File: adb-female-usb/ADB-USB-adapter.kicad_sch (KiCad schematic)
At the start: 2 parts

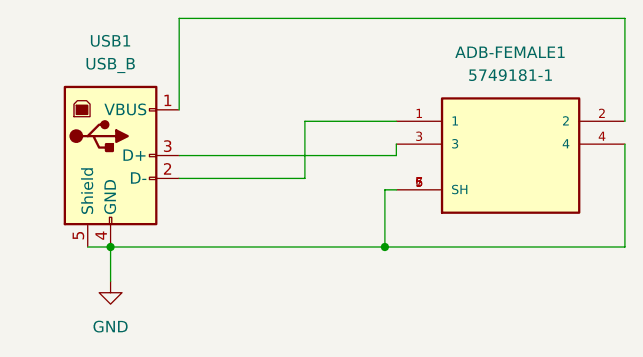
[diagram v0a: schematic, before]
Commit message: switched D+/D- on USB PCB, isolated shield from ground
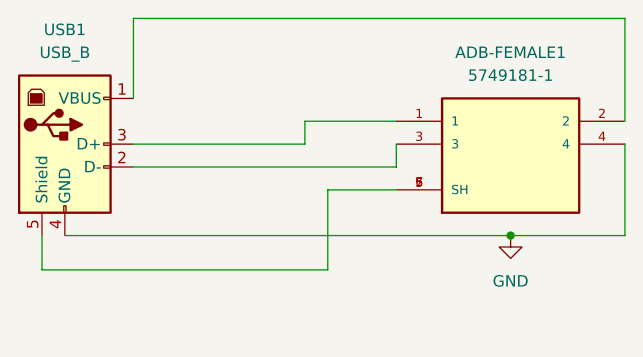
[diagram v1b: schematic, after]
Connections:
- net GND: no longer ADB-FEMALE1.5 (SH), ADB-FEMALE1.6 (SH), ADB-FEMALE1.7 (SH), USB1.5 (Shield)
- net at USB1.2 (D-): now also ADB-FEMALE1.3; no longer ADB-FEMALE1.1
- net at USB1.3 (D+): now also ADB-FEMALE1.1; no longer ADB-FEMALE1.3
- new net: ADB-FEMALE1.5 (SH), ADB-FEMALE1.6 (SH), ADB-FEMALE1.7 (SH), USB1.5 (Shield)
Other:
- moved on the sheet: USB1
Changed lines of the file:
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@@
 (kicad_sch (version 20230121) (generator eeschema)
   (paper "A4")
-  (junction (at 41.91 46.99) (diameter 0) (color 0 0 0 0)
+  (junction (at 86.36 45.72) (diameter 0) (color 0 0 0 0)
   )
-  (junction (at 72.39 46.99) (diameter 0) (color 0 0 0 0)
-  )
-  (wire (pts (xy 39.37 46.99) (xy 41.91 46.99))
+  (wire (pts (xy 86.36 45.72) (xy 36.83 45.72))
     (stroke (width 0) (type default))
   )
@@
     (stroke (width 0) (type default))
   )
-  (wire (pts (xy 63.5 39.37) (xy 63.5 33.02))
+  (wire (pts (xy 99.06 45.72) (xy 86.36 45.72))
     (stroke (width 0) (type default))
   )
-  (wire (pts (xy 49.53 31.75) (xy 49.53 21.59))
+  (wire (pts (xy 44.45 30.48) (xy 44.45 21.59))
     (stroke (width 0) (type default))
   )
-  (wire (pts (xy 72.39 46.99) (xy 99.06 46.99))
+  (wire (pts (xy 66.04 49.53) (xy 34.29 49.53))
     (stroke (width 0) (type default))
   )
@@
     (stroke (width 0) (type default))
   )
-  (wire (pts (xy 49.53 36.83) (xy 73.66 36.83))
+  (wire (pts (xy 63.5 35.56) (xy 44.45 35.56))
     (stroke (width 0) (type default))
   )
-  (wire (pts (xy 41.91 46.99) (xy 72.39 46.99))
+  (wire (pts (xy 66.04 40.64) (xy 73.66 40.64))
     (stroke (width 0) (type default))
   )
-  (wire (pts (xy 41.91 46.99) (xy 41.91 50.8))
+  (wire (pts (xy 34.29 49.53) (xy 34.29 45.72))
     (stroke (width 0) (type default))
   )
-  (wire (pts (xy 73.66 36.83) (xy 73.66 35.56))
+  (wire (pts (xy 66.04 40.64) (xy 66.04 49.53))
     (stroke (width 0) (type default))
   )
-  (wire (pts (xy 72.39 40.64) (xy 72.39 46.99))
+  (wire (pts (xy 44.45 21.59) (xy 99.06 21.59))
     (stroke (width 0) (type default))
   )
-  (wire (pts (xy 73.66 40.64) (xy 72.39 40.64))
+  (wire (pts (xy 63.5 33.02) (xy 63.5 35.56))
     (stroke (width 0) (type default))
   )
-  (wire (pts (xy 49.53 39.37) (xy 63.5 39.37))
+  (wire (pts (xy 73.66 38.1) (xy 73.66 35.56))
     (stroke (width 0) (type default))
   )
-  (wire (pts (xy 99.06 46.99) (xy 99.06 35.56))
+  (wire (pts (xy 44.45 38.1) (xy 73.66 38.1))
     (stroke (width 0) (type default))
   )
-  (wire (pts (xy 49.53 21.59) (xy 99.06 21.59))
+  (wire (pts (xy 99.06 35.56) (xy 99.06 45.72))
     (stroke (width 0) (type default))
   )
-  (symbol (lib_id "power:GND") (at 41.91 50.8 0) (unit 1)
+  (symbol (lib_id "power:GND") (at 86.36 45.72 0) (unit 1)
     (in_bom yes) (on_board yes) (dnp no) (fields_autoplaced)
-    (property "Reference" "#PWR01" (at 41.91 57.15 0)
+    (property "Reference" "#PWR01" (at 86.36 52.07 0)
       (effects (font (size 1.27 1.27)) hide)
     )
-    (property "Value" "GND" (at 41.91 55.88 0)
+    (property "Value" "GND" (at 86.36 50.8 0)
       (effects (font (size 1.27 1.27)))
     )
-    (property "Footprint" "" (at 41.91 50.8 0)
+    (property "Footprint" "" (at 86.36 45.72 0)
       (effects (font (size 1.27 1.27)) hide)
     )
-    (property "Datasheet" "" (at 41.91 50.8 0)
+    (property "Datasheet" "" (at 86.36 45.72 0)
       (effects (font (size 1.27 1.27)) hide)
     )
@@
     )
   )
-  (symbol (lib_id "Connector:USB_B") (at 41.91 36.83 0) (unit 1)
+  (symbol (lib_id "Connector:USB_B") (at 36.83 35.56 0) (unit 1)
     (in_bom yes) (on_board yes) (dnp no) (fields_autoplaced)
-    (property "Reference" "USB1" (at 41.91 24.13 0)
+    (property "Reference" "USB1" (at 36.83 22.86 0)
       (effects (font (size 1.27 1.27)))
     )
-    (property "Value" "USB_B" (at 41.91 26.67 0)
+    (property "Value" "USB_B" (at 36.83 25.4 0)
       (effects (font (size 1.27 1.27)))
     )
-    (property "Footprint" "Connector_USB:USB_B_OST_USB-B1HSxx_Horizontal" (at 45.72 38.1 0)
+    (property "Footprint" "Connector_USB:USB_B_OST_USB-B1HSxx_Horizontal" (at 40.64 36.83 0)
       (effects (font (size 1.27 1.27)) hide)
     )
-    (property "Datasheet" " ~" (at 45.72 38.1 0)
+    (property "Datasheet" " ~" (at 40.64 36.83 0)
       (effects (font (size 1.27 1.27)) hide)
     )
